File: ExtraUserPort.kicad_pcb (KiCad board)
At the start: 2 copper layers, 60.8 x 99.9 mm, 21 parts, among them CN1 EXPANSION_PORT, CN2 ALMOST_USERPORT, CN3 DB9_MALE, J1 ATTENTION, U1 GAL16V8, U2 MOS_6529, U3 W65C51S, U4 74HCT04, U5 MAX238, Y1 1.8432M

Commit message: Fix some warnings
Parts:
- moved C6 117.3 mm to (135.7, 67.3), turned to 180 degrees
- moved C5 116.2 mm to (140.1, 67.3)
- moved C9 112.8 mm to (142.1, 84.6), turned to 180 degrees
- moved C7 107.5 mm to (133.8, 84.6)
- moved J1 106.3 mm to (127.3, 64.8)
- moved C8 97.3 mm to (148.4, 67.3), turned to 180 degrees
- moved C2 94.0 mm to (128.4, 118.9)
- moved R1 85.0 mm to (153.8, 63.5)
- moved R2 85.0 mm to (153.8, 67.3)
- moved U2 84.1 mm to (134.7, 114.9), turned to 180 degrees
- moved C4 79.7 mm to (146.2, 85.9), turned to 270 degrees
- moved Y1 78.5 mm to (158.6, 117.5), turned to 180 degrees
- moved U4 67.8 mm to (150.0, 92.2), turned to 90 degrees
- moved U5 52.7 mm to (160.1, 72.1), turned to 270 degrees
- moved U3 49.0 mm to (142.4, 112.4), turned to 90 degrees
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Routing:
- net /p1: track 0.00 -> 65.9 mm, vias 0 -> 1
- net /p6: track 0.00 -> 55.6 mm, vias 0 -> 1
- net /~dcd_ttl: track 0.00 -> 34.2 mm, vias 0 -> 1
- net +5V: track 36.3 -> 61.3 mm
- net /~dsr_ttl: track 0.00 -> 23.5 mm, vias 0 -> 1
- net Net-(C6-Pad1): track 0.00 -> 5.49 mm
- net Net-(C6-Pad2): track 0.00 -> 5.46 mm
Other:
- outline, holes or cut-outs redrawn

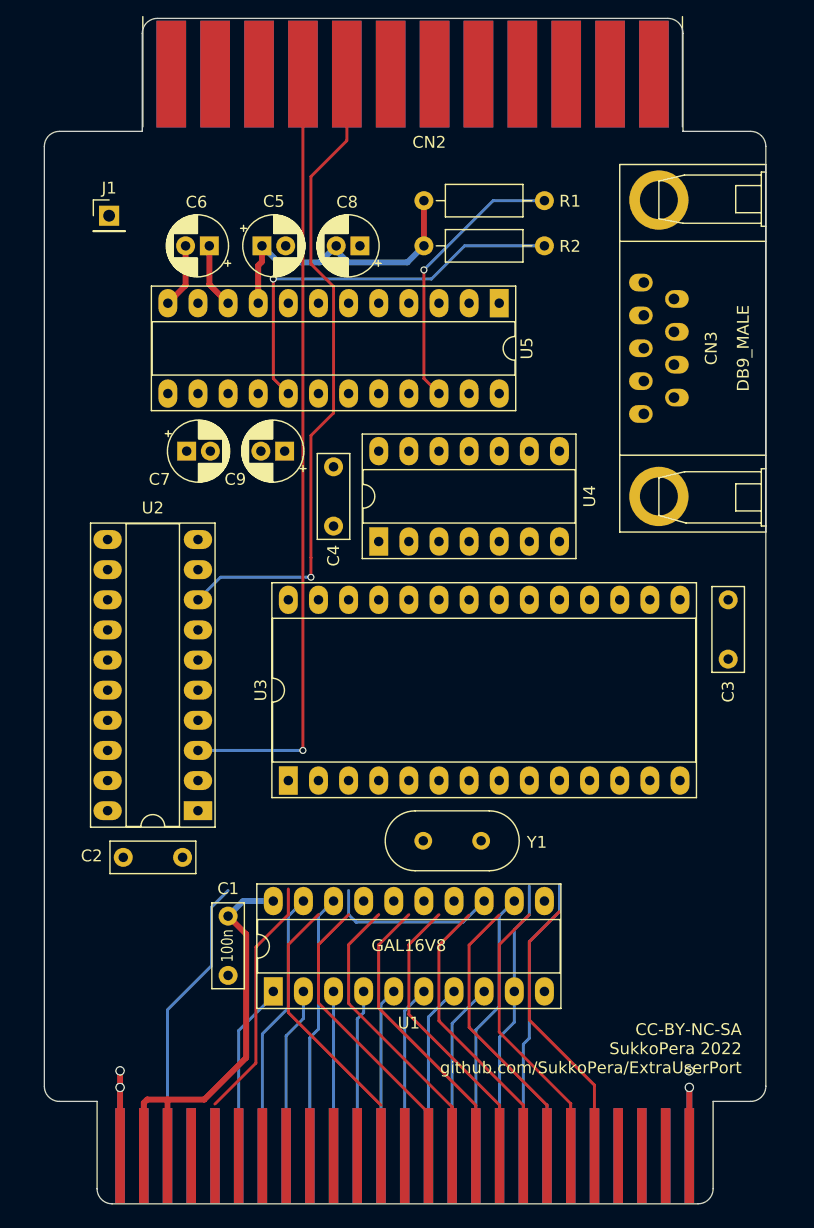
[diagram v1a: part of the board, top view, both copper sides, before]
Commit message: (Very) Rough routing done
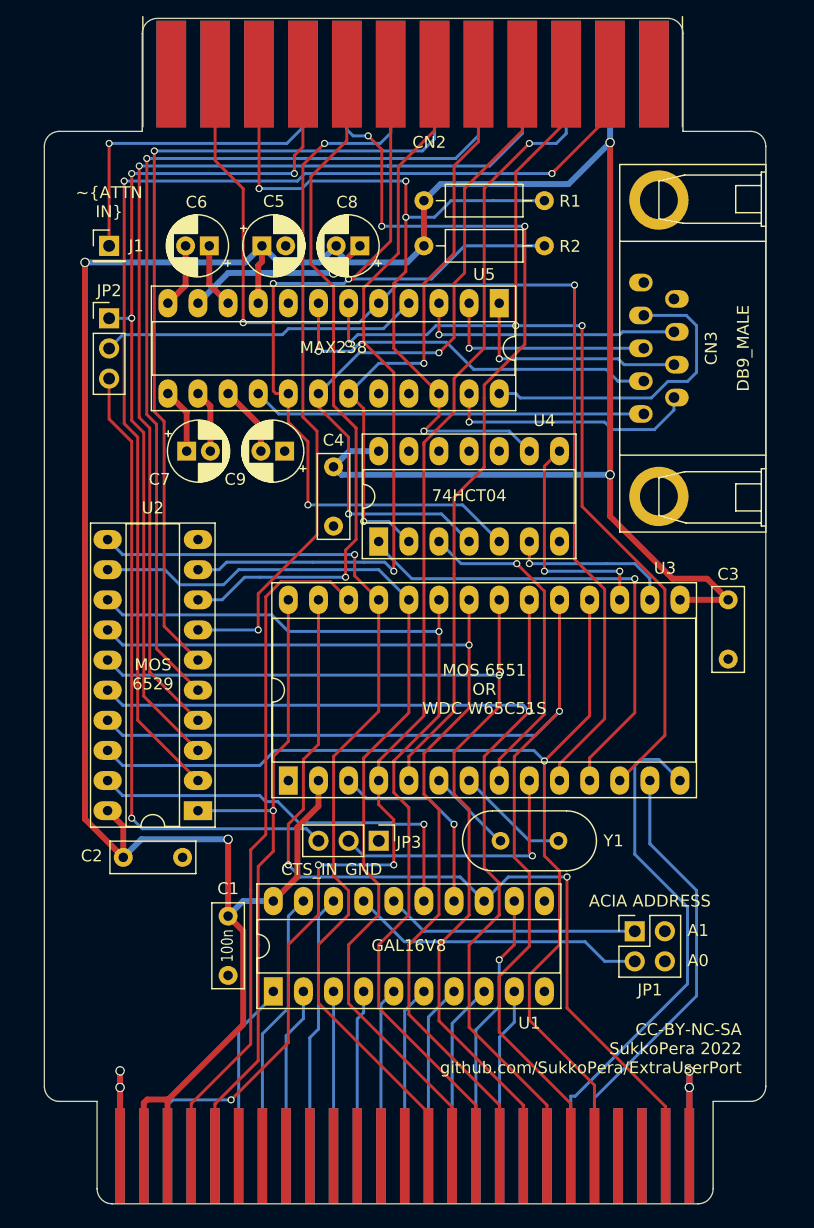
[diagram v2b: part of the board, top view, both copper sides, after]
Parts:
- added JP1: JMP_ACIA_ADDR, Connector_PinHeader_2.54mm:PinHeader_2x02_P2.54mm_Vertical, F.Cu at (171.6, 125.1)
- added JP2: JMP_CTS_IN, Connector_PinHeader_2.54mm:PinHeader_1x03_P2.54mm_Vertical, F.Cu at (127.3, 73.4)
- added JP3: JMP_CTS_ACIA, Connector_PinHeader_2.54mm:PinHeader_1x03_P2.54mm_Vertical, F.Cu at (150.0, 117.5)
- J1: value ATTENTION -> ATTENTION_IN
- U3: value W65C51S -> MOS_6551_ACIA
- moved Y1 6.51 mm to (165.1, 117.5)
- moved J1 2.54 mm to (127.3, 67.3)
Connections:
- CN1 pad 5: /r_w~ -> /r_~w
- CN2 pad 8: (no net) -> /rxc_ttl
- CN2 pad C: (no net) -> /rxd_ttl
- CN2 pad D: (no net) -> /~rts_ttl
- CN2 pad E: (no net) -> /~dtr_ttl
- CN2 pad H: (no net) -> /~dcd_ttl
- CN2 pad L: (no net) -> /~dsr_ttl
- CN2 pad M: (no net) -> /txd_ttl
- CN3 pad 1: (no net) -> /~dcd
- U1 pad 16: (no net) -> /bit1
- U1 pad 17: (no net) -> /bit0
- U2 pad 1: /r_w~ -> /r_~w
- U3 pad 28: /r_w~ -> /r_~w
- U3 pad 5: (no net) -> /rxc_ttl
- U3 pad 9: /~cts_ttl -> Net-(JP3-Pad2)
- U5 pad 16: (no net) -> /~dcd
- U5 pad 4: /~cts_ttl -> Net-(JP2-Pad2)
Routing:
- net +5V: track 61.3 -> 258.4 mm, vias 0 -> 4
- net /p0: track 0.00 -> 100.1 mm, vias 0 -> 2
- net /txd_ttl: track 0.00 -> 95.6 mm, vias 0 -> 2
- net /~reset: track 24.5 -> 114.1 mm, vias 0 -> 4
- net /rxd_ttl: track 0.00 -> 89.5 mm, vias 0 -> 3
- net /p2: track 0.00 -> 87.2 mm, vias 0 -> 1
- net /p3: track 0.00 -> 80.6 mm, vias 0 -> 1
- net /rxc_ttl: track 0.00 -> 77.6 mm, vias 0 -> 3
- net /p4: track 0.00 -> 74.0 mm, vias 0 -> 1
- net /d1: track 23.9 -> 92.0 mm, vias 0 -> 1
- net /d0: track 23.9 -> 90.5 mm, vias 0 -> 1
- net /d2: track 24.1 -> 89.0 mm, vias 0 -> 1
- net /~rts_ttl: track 0.00 -> 64.6 mm, vias 0 -> 2
- net /p7: track 0.00 -> 62.5 mm, vias 0 -> 1
- net /d3: track 24.3 -> 86.5 mm, vias 0 -> 1
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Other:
- board text added: "A0"
- board text added: "A1"
- board text added: "ACIA ADDRESS"
- board text added: "CTS_IN"
- board text added: "GND"
- board text added: "MOS 6529"
- board text added: "MOS 6551 OR WDC W65C51S"
- board text added: "~ATTN IN"

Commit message: Improve routing
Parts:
- removed C4: 100n, Capacitor_THT:C_Disc_D7.0mm_W2.5mm_P5.00mm
- removed U4: 74HCT04, Package_DIP:DIP-14_W7.62mm_Socket_LongPads
- added R3: 10k, Resistor_THT:R_Axial_DIN0207_L6.3mm_D2.5mm_P10.16mm_Horizontal, F.Cu at (150.0, 92.3)
- moved R1 21.5 mm to (150.0, 84.7)
- moved R2 21.5 mm to (150.0, 88.5)
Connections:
- R1 pad 2: /~dsr_ttl -> /~dcd_ttl
- R2 pad 2: /~dcd_ttl -> /~dsr_ttl
- U3 pad 11: Net-(U3-Pad11) -> /~dtr_ttl
- U3 pad 16: Net-(U3-Pad16) -> /~dcd_ttl
- U3 pad 17: Net-(U3-Pad17) -> /~dsr_ttl
- U3 pad 8: Net-(U3-Pad8) -> /~rts_ttl
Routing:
- net /~cts_ttl: track 54.4 -> 96.4 mm, vias 1 -> 3
- net Net-(U3-Pad11): track 41.7 -> 0.00 mm, vias 1 -> 0
- net /~dtr_ttl: track 49.5 -> 87.4 mm, vias 2 -> 4
- net /~rts_ttl: track 64.6 -> 97.8 mm, vias 2 -> 3
- net Net-(U3-Pad8): track 28.2 -> 0.00 mm, vias 1 -> 0
- net Net-(U3-Pad17): track 19.7 -> 0.00 mm, vias 2 -> 0
- net Net-(U3-Pad16): track 14.3 -> 0.00 mm, vias 1 -> 0
- net +5V: track 258.4 -> 270.2 mm, vias 4 -> 5
- net /~dsr_ttl: track 67.8 -> 78.3 mm
- net /p5: track 60.3 -> 70.4 mm
- net /d0: track 90.5 -> 100.3 mm, vias 1 -> 0
- net /~dcd_ttl: track 81.0 -> 89.8 mm, vias 3 -> 4
- net /p7: track 62.5 -> 70.3 mm
- net /p6: track 58.9 -> 66.6 mm
- net /phi2: track 75.9 -> 81.2 mm
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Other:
- board text added: "MOS 6551/8551 OR WDC W65C51S"
- board text removed: "MOS 6551 OR WDC W65C51S"

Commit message: Almost there
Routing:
- net GND: track 28.6 -> 52.0 mm, vias 4 -> 6
- net +5V: track 270.2 -> 253.1 mm
- net /~dcd_ttl: track 89.8 -> 82.5 mm
- net /txd_ttl: track 99.1 -> 92.2 mm
- net /~dsr_ttl: track 78.3 -> 75.1 mm
- net /~rts: track 19.0 -> 21.1 mm
- net /p7: track 70.3 -> 68.2 mm
- net /rxc_ttl: track 77.5 -> 79.3 mm
- net /~rts_ttl: track 97.8 -> 96.0 mm
- net Net-(JP2-Pad2): track 26.9 -> 28.6 mm, vias 0 -> 1
- net Net-(CN2-Pad9): track 30.0 -> 31.5 mm, vias 1 -> 4
- net /~dtr_ttl: track 87.4 -> 88.5 mm
- net /~cts: track 22.1 -> 22.9 mm
- net /p5: track 70.4 -> 71.1 mm, vias 2 -> 4
- net /p3: track 80.6 -> 81.3 mm, vias 1 -> 3
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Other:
- board text added: "P0"
- board text added: "P1"
- board text added: "P6"
- board text added: "P7"
- board text added: "RXD"
- board text added: "TXD"
- board text added: "~DCD"
- board text added: "~DSR"
- board text added: "~DTR"
- board text added: "~RTS"

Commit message: Swap top/bottom pins of edge connector Sigh...
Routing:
- net /p2: track 87.3 -> 94.3 mm, vias 3 -> 2
- net /~rts_ttl: track 96.0 -> 91.7 mm, vias 3 -> 4
- net /p0: track 99.9 -> 103.1 mm, vias 2 -> 3
- net /rxc_ttl: track 79.3 -> 78.3 mm, vias 3 -> 2
- net Net-(CN2-Pad9): track 31.5 -> 30.7 mm, vias 4 -> 3
- net /rxd_ttl: track 89.3 -> 89.8 mm, vias 2 -> 3
- net /p5: track 71.1 -> 71.6 mm, vias 4 -> 3
- net /p4: track 74.2 -> 74.6 mm, vias 3 -> 2
- net /p3: track 81.3 -> 81.7 mm, vias 3 -> 2
- net /p1: track 75.7 -> 75.4 mm, vias 3 -> 4
- net /~dsr_ttl: track 75.1 -> 75.2 mm, vias 4 -> 5
- net /txd_ttl: track 92.2 -> 92.3 mm, vias 2 -> 3
- net +5V: vias 5 -> 4
- net /~dtr_ttl: vias 4 -> 5
- net /p6: vias 1 -> 2
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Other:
- board text added: "+5V"
- board text added: "NC"
- board text added: "P2"
- board text added: "P3"
- board text added: "P4"
- board text added: "P5"
- board text added: "RXC"
- board text added: "~ATTN"
- board text added: "~RESET"

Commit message: WIP
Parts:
- moved JP3 25.8 mm to (141.1, 93.2), turned to 90 degrees
- moved JP2 22.1 mm to (141.1, 90.7), turned to 90 degrees
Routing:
- net /~cts_ttl: track 96.4 -> 18.2 mm, vias 3 -> 0
- net Net-(JP3-Pad2): track 24.3 -> 43.6 mm, vias 1 -> 2
- net Net-(JP2-Pad2): track 28.6 -> 35.7 mm
- net /p0: track 103.1 -> 100.2 mm
- net /rxd_ttl: track 89.8 -> 87.5 mm
- net /~cs_par: track 35.3 -> 37.1 mm
- net /~dcd_ttl: track 82.5 -> 80.9 mm
- net /txd_ttl: track 92.3 -> 93.1 mm, vias 3 -> 4
- net /~dsr_ttl: track 75.2 -> 74.6 mm
- net +5V: track 253.1 -> 252.5 mm
- net /~dtr_ttl: track 88.5 -> 88.0 mm
- net Net-(CN2-Pad9): track 30.7 -> 30.4 mm, vias 3 -> 2
- net GND: vias 6 -> 12
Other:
- board text removed: "CTS_IN"

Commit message: WIP
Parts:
- JP1: value JMP_ACIA_ADDR -> JMP_ADDRESS; footprint Connector_PinHeader_2.54mm:PinHeader_2x02_P2.54mm_Vertical -> Connector_PinHeader_2.54mm:PinHeader_1x03_P2.54mm_Vertical
- U1: value GAL16V8 -> GAL20V8; footprint Package_DIP:DIP-20_W7.62mm_Socket_LongPads -> Package_DIP:DIP-24_W7.62mm_Socket_LongPads
- moved JP1 2.94 mm to (174.4, 126.0), turned to 90 degrees
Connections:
- JP1 pad 1: /bit1 -> GND
- JP1 pad 2: GND -> Net-(JP1-Pad2)
- JP1 pad 3: /bit0 -> +5V
- U1 pad 10: GND -> /a6
- U1 pad 11: (no net) -> /a5
- U1 pad 12: /a5 -> GND
- U1 pad 13: /phi2 -> /a4
- U1 pad 14: /~cs_ser -> Net-(JP1-Pad2)
- U1 pad 15: /~cs_par -> /~cs_ser
- U1 pad 16: /bit1 -> /~cs_par
- U1 pad 17: /bit0 -> (no net)
- U1 pad 18: /a12 -> (no net)
- U1 pad 19: /a14 -> /r_~w
- U1 pad 2: /a13 -> /a14
- U1 pad 20: +5V -> (no net)
- U1 pad 3: /a11 -> /a13
- U1 pad 4: /a10 -> /a12
- U1 pad 5: /a9 -> /a11
- U1 pad 6: /a8 -> /a10
- U1 pad 7: /a7 -> /a9
- U1 pad 8: /a6 -> /a8
- U1 pad 9: /a4 -> /a7
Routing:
- net /a1: track 40.1 -> 0.00 mm, vias 2 -> 0
- net /a0: track 36.2 -> 0.00 mm, vias 2 -> 0
- net +5V: track 252.5 -> 284.5 mm
- net /bit0: track 26.0 -> 0.00 mm
- net /bit1: track 21.5 -> 0.00 mm
- net /r_~w: track 56.4 -> 72.1 mm, vias 1 -> 3
- net Net-(JP1-Pad2): track 0.00 -> 11.8 mm
- net /a4: track 14.4 -> 25.1 mm, vias 0 -> 1
- net /~cs_par: track 37.1 -> 44.9 mm
- net /a14: track 22.9 -> 15.3 mm
- net /~cs_ser: track 17.7 -> 25.0 mm
- net /a12: track 22.3 -> 15.7 mm
- net /a5: track 23.2 -> 17.3 mm, vias 1 -> 0
- net /phi2: track 81.2 -> 78.9 mm
- net /d7: track 83.1 -> 81.0 mm
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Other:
- board text added: "ADDRESS"
- board text added: "EXT"
- board text added: "INT"
- board text removed: "A0"
- board text removed: "A1"
- board text removed: "ACIA ADDRESS"

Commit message: WIP
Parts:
- added U4: 74LS652, Package_DIP:DIP-24_W7.62mm_Socket_LongPads, F.Cu at (131.6, 130.2)
- moved C2 15.7 mm to (133.4, 133.7), turned to 180 degrees
- moved U2 10.2 mm to (134.7, 125.1)
- moved JP1 5.86 mm to (179.5, 128.9), turned to 180 degrees
- moved C7 3.81 mm to (137.6, 84.6)
- moved C9 3.81 mm to (145.9, 84.6)
- moved U1 3.81 mm to (144.9, 130.2)
- moved C1 3.56 mm to (140.8, 123.8)
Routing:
- net +5V: track 284.5 -> 264.0 mm, vias 4 -> 3
- net /a1: track 0.00 -> 13.4 mm
- net /a0: track 0.00 -> 11.2 mm
- net /p0: track 100.2 -> 93.1 mm
- net /p1: track 75.4 -> 69.0 mm
- net /p2: track 94.3 -> 88.6 mm
- net /p3: track 81.7 -> 76.7 mm
- net /~cs_ser: track 25.0 -> 29.8 mm
- net /p4: track 74.6 -> 70.5 mm
- net /d3: track 88.6 -> 85.2 mm
- net /~reset: track 110.9 -> 114.2 mm
- net /phi2: track 78.9 -> 75.7 mm
- net /a4: track 25.1 -> 28.3 mm
- net /a5: track 17.3 -> 20.4 mm
- net /d2: track 91.7 -> 88.6 mm
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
